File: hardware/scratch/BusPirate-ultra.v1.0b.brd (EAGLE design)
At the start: 100 x 50 mm, 179 parts, among them IC1 23LC1024, IC10 SN74LVC1T45DBV, IC11 SN74LVC1T45DBV, IC12 74LVC1G07DBV, IC13 SN74LVC1T45DBV, IC17 74LVC1G07DBV, IC18 SN74LVC1T45DBV, IC19 74LVC1G07DBV, IC2 23LC1024, IC20 SN74LVC1T45DBV, IC21 74LVC1G07DBV, IC22 SN74LVC1T45DBV, IC23 MCP1824_ADJ, IC24 74HCT4051, IC3 74AC573, IC4 74LVC1G07DBV, IC5 74LVC1G07DBV, IC6 74LVC1G07DBV, IC7 74LVC1G07DBV, IC8 SN74LVC1T45DBV, IC9 SN74LVC1T45DBV, J2 CON_HEADER_1X04, J4 CON_HEADER_1X10-RIGHT_ANGLED_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, Q1 DMMT3906W, U1 W25X40CL, U2 STM32F103ZX, U3 ICE40HX4K, U4 MCP6001, U5 MCP4442, U6 MCP4442, U7 MCP6001

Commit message: change buffer 573 to 244, replaced MCP4446 digital pot back to 4066 analog switch
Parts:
- removed IC3: 74AC573, dp_devices:TSSOP-20
- removed R49, R52: 10K, dp_devices.v6:R603
- added U8: 74HCT4066PW, dp_devices.v6:TSSOP-14
- U5: value MCP4442 -> 74LVC245A; device dp_devices.v6:TSSOP-14 -> dp_devices.v6:TSSOP-20
- U9: value MCP4442 -> 74HCT4066PW
- moved U5 24.3 mm to (76.8, 23.5), turned to 270 degrees
- turned U9 to 0 degrees
- renumbered U6 to U9
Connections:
- removed net MCU_I2C_SCL: R49.1, U2.136, U5.4, U9.4
- removed net MCU_I2C_SDA: R52.1, U2.137, U5.5, U9.5
- removed net N$47: RN3.2, U9.13
- removed net N$48: RN3.4, U9.2
- removed net V33PU: U2.56
- removed net V50PU: U2.57
- new net MCU_VPU: U2.56, U8.12, U8.13, U8.5, U8.6, U9.12, U9.13, U9.5, U9.6
- new net N$33: RN3.3, U9.1
- new net N$45: RN3.4, U9.11
- net 3V3: now also U5.20; no longer IC3.11, IC3.20, R49.2, R52.2, U9.3
- net BPIO0: now also U5.11; no longer IC3.2
- net BPIO1: now also U5.12; no longer IC3.3
- net BPIO2: now also U5.13; no longer IC3.4
- net BPIO3: now also U5.14; no longer IC3.5
- net BPIO4: now also U5.15; no longer IC3.6
- net BPIO5: now also U5.16; no longer IC3.7
- net BPIO6: now also U5.17; no longer IC3.8
- net BPIO7: now also U5.18; no longer IC3.9
- net GND: now also U5.1, U5.10, U5.19, U8.7, U9.7; no longer IC3.1, IC3.10, U5.11, U5.3, U5.6, U9.11, U9.6
- net LAT0: now also U5.9; no longer IC3.19
- net LAT1: now also U5.8; no longer IC3.18
- net LAT2: now also U5.7; no longer IC3.17
- net LAT3: now also U5.6; no longer IC3.16
- net LAT4: now also U5.5; no longer IC3.15
- net LAT5: now also U5.4; no longer IC3.14
- net LAT6: now also U5.3; no longer IC3.13
- net LAT7: now also U5.2; no longer IC3.12
- net N$2: now also U8.1; no longer U5.10
- net N$3: now also U8.4; no longer U5.7
- net N$4: now also U8.8; no longer U5.13
- net N$42: now also RN3.1, U9.4; no longer RN3.3, U9.10
- net N$44: now also RN3.2, U9.8; no longer RN3.1, U9.7
- net N$5: now also U8.11; no longer U5.2
- net VREF/VOUT: now also U8.10, U8.2, U8.3, U8.9, U9.10, U9.2, U9.3; no longer U5.1, U5.14, U5.8, U5.9, U9.1, U9.14, U9.8
- net VUSB: now also U8.14, U9.14; no longer U5.12, U9.12
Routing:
- net V33PU: track 35.2 -> 0.00 mm, vias 1 -> 0
- net V50PU: track 24.5 -> 0.00 mm, vias 1 -> 0
- net MCU_I2C_SCL: track 11.7 -> 0.00 mm
- net MCU_I2C_SDA: track 8.41 -> 0.00 mm

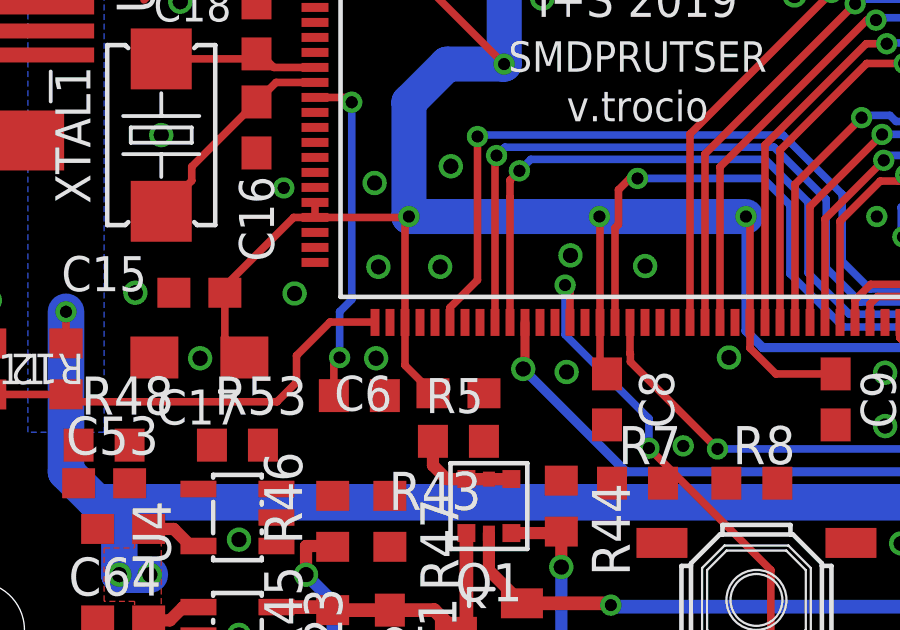
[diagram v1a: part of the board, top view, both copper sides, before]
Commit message: move MCU_AUX12 to pin 55, reserve MCU 41-43 pins for display
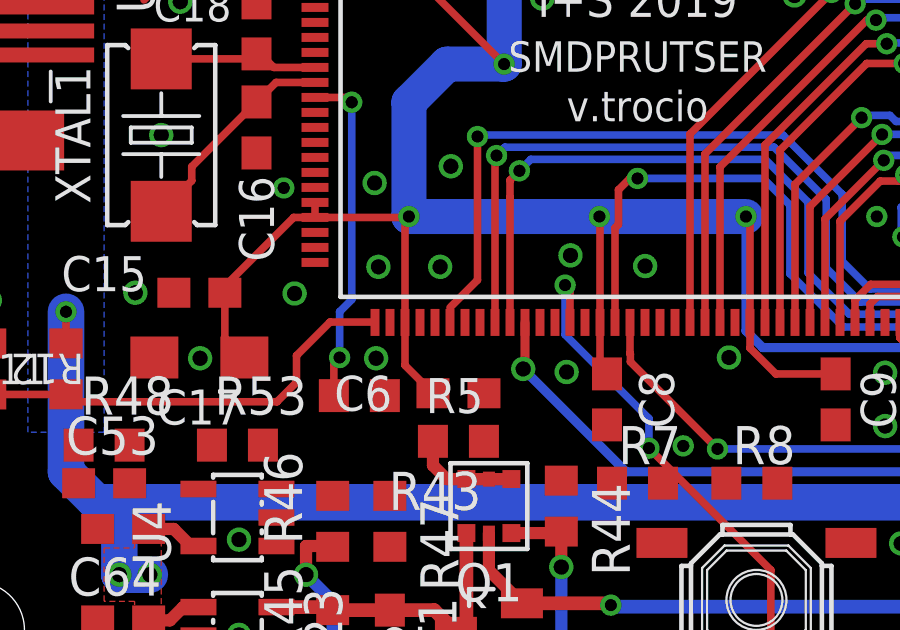
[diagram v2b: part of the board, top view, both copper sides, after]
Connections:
- net ADC2 renamed DISPLAY_SPI_MOSI
- removed net VEXTPU: U2.55
- new net DISPLAY_SPI_CLOCK: U2.41
- new net DISPLAY_SPI_MISO: U2.42
- net MCU_AUX12: now also U2.55; no longer U2.42
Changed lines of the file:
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@@
 <wire x1="61.595" y1="9.271" x2="47.625" y2="2.96" width="0" layer="19" extent="1-16"/>
-</signal>
-<signal name="ADC2">
-<contactref element="U2" pad="43"/>
 </signal>
 <signal name="N$6">
@@
 <wire x1="56.515" y1="6.604" x2="57.15" y2="5.969" width="0.6096" layer="16"/>
 </signal>
-<signal name="VEXTPU">
-<contactref element="U2" pad="55"/>
-</signal>
 <signal name="UART_RX">
 <contactref element="TP2" pad="TP"/>
@@
 <signal name="MCU_AUX12">
 <contactref element="U3" pad="41"/>
-<contactref element="U2" pad="42"/>
 <wire x1="47.3393" y1="14.25" x2="47.3393" y2="15.3987" width="0.254" layer="1"/>
 <wire x1="47.3393" y1="15.3987" x2="46.736" y2="16.002" width="0.254" layer="1"/>
@@
 <wire x1="19.785" y1="14.74513125" x2="20.701" y2="15.66113125" width="0.254" layer="1"/>
 <wire x1="20.701" y1="20.447" x2="20.701" y2="15.66113125" width="0.254" layer="1"/>
-<wire x1="19.785" y1="14.25" x2="19.785" y2="14.74513125" width="0.254" layer="1"/>
 <via x="20.701" y="20.447" extent="1-16" drill="0.4064"/>
 <wire x1="32.8581375" y1="18.523075" x2="30.8834125" y2="20.4978" width="0.254" layer="16"/>
@@
 <wire x1="20.751796875" y1="20.4978" x2="20.701" y2="20.447" width="0.254" layer="16"/>
 <wire x1="46.736" y1="16.002" x2="46.736" y2="16.04066875" width="0.254" layer="16"/>
+<contactref element="U2" pad="55"/>
+<wire x1="20.701" y1="15.66113125" x2="26.285" y2="14.25" width="0" layer="19" extent="1-1"/>
 </signal>
 <signal name="VREF/VOUT">
@@
 <wire x1="26.785" y1="14.25" x2="88.87" y2="9.25" width="0" layer="19" extent="1-1"/>
 </signal>
+<signal name="DISPLAY_SPI_CLOCK">
+<contactref element="U2" pad="41"/>
+</signal>
+<signal name="DISPLAY_SPI_MOSI">
+<contactref element="U2" pad="43"/>
+</signal>
+<signal name="DISPLAY_SPI_MISO">
+<contactref element="U2" pad="42"/>
+</signal>
 </signals>

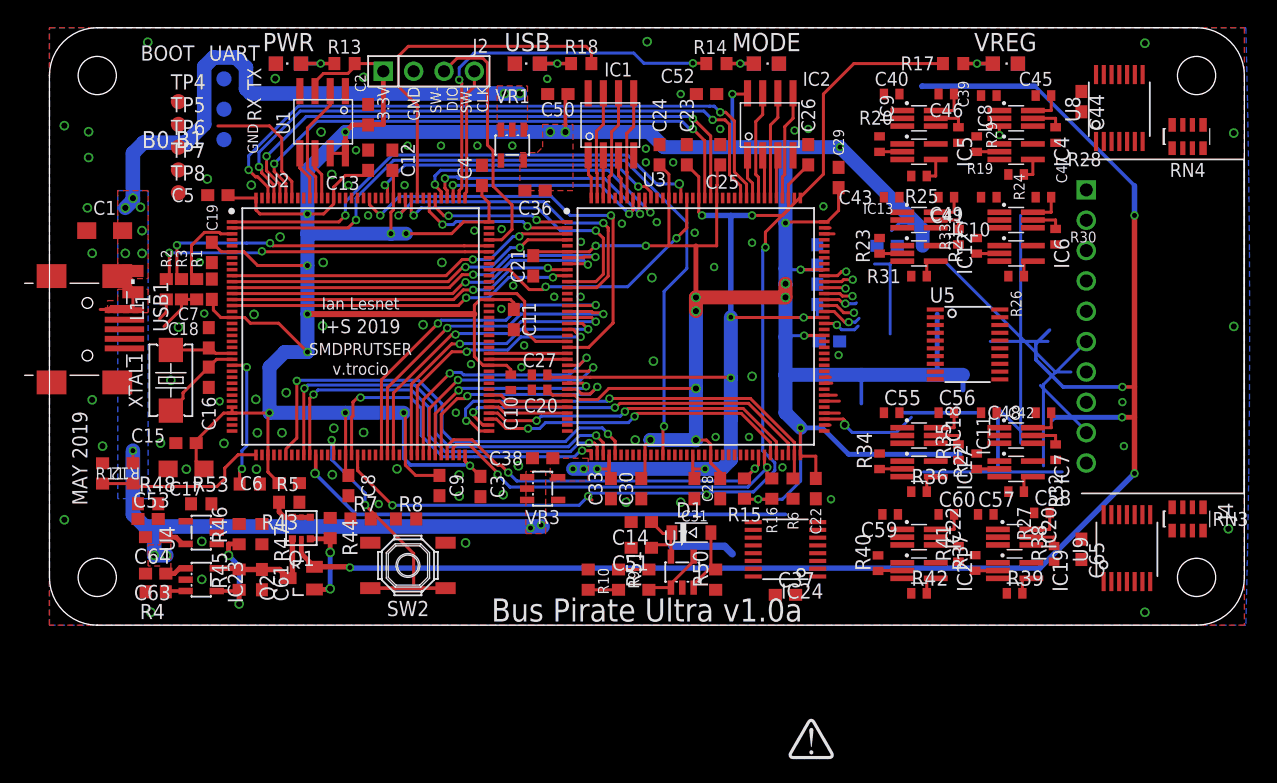
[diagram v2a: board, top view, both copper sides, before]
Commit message: changes in FPGA pin connection *BANK 1
BUFOD0 102
BUFIO0 104
BUFDIR0 101

BUFOD1 106
BUFIO1 107
BUFDIR1 105

BUFOD2 95
BUFIO2 96
BUFDIR2 94

BUFOD3 98
BUFIO3 99
BUFDIR3 97

BUFOD4 80
BUFIO4 81
BUFDIR4 82

BUFOD5 76
BUFIO5 78
BUFDIR5 79

BUFOD6 73
BUFIO6 74
BUFDIR6 75

LAT0 93
LAT1 91
LAT2 90
LAT3 88
LAT4 87
LAT5 85
LAT6 84
LAT7 83

*BANK 2

BUFOD7 62
BUFIO7 63
BUFDIR7 64

ADC_MUX_EN 61
ADC_MUX_S2 60
ADC_MUX_S1 56
ADC_MUX_S0 55
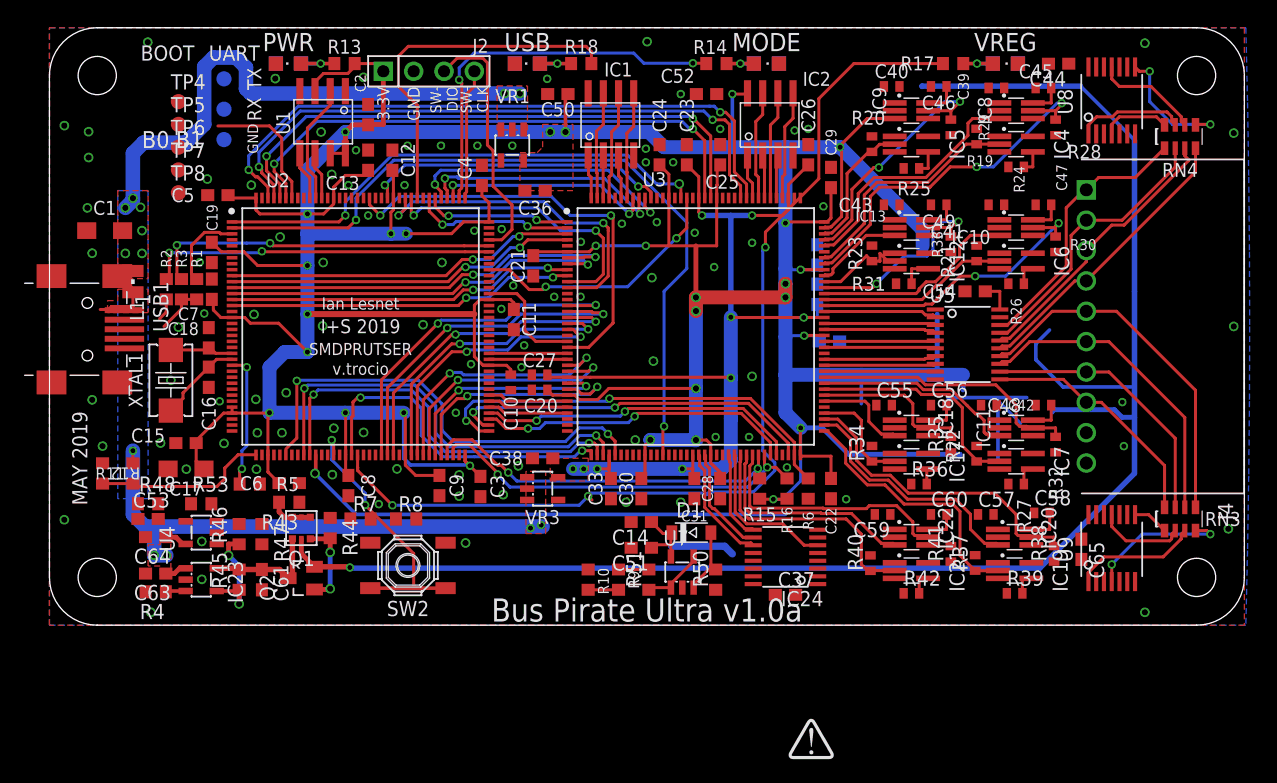
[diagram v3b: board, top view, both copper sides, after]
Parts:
- moved C54 8.29 mm to (77.5, 27.9), flipped to the top
- moved C44 3.70 mm to (84.5, 47.0), turned to 180 degrees
- moved R31 1.42 mm to (71.5, 28.6)
- moved R15 1.27 mm to (59.4, 11.4)
- moved R16 1.27 mm to (61.7, 11.4)
- moved R6 1.27 mm to (63.5, 11.4)
- moved C22 1.27 mm to (65.4, 11.4)
- moved U9 1.27 mm to (88.9, 6.35)
- moved IC18 0.90 mm to (72.1, 16.5)
- moved IC17 0.90 mm to (72.1, 13.7)
- moved C39 0.90 mm to (79.2, 45.0)
- moved C41 0.90 mm to (79.2, 35.2)
- moved C46 0.90 mm to (74.4, 45.1)
- moved C49 0.90 mm to (74.4, 35.2)
- moved C55 0.90 mm to (69.8, 18.4)
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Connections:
- net ADC_MUX_EN: now also U3.61; no longer U3.45
- net ADC_MUX_S0: now also U3.55; no longer U3.42
- net ADC_MUX_S1: now also U3.56; no longer U3.43
- net ADC_MUX_S2: now also U3.60; no longer U3.44
- net BPIO0: now also U5.18; no longer U5.11
- net BPIO1: now also U5.17; no longer U5.12
- net BPIO2: now also U5.16; no longer U5.13
- net BPIO3: now also U5.15; no longer U5.14
- net BPIO4: now also RN3.5, U5.14; no longer RN3.6, U5.15
- net BPIO5: now also RN3.6, U5.13; no longer RN3.8, U5.16
- net BPIO6: now also U5.12; no longer U5.17
- net BPIO7: now also RN3.8, U5.11; no longer RN3.5, U5.18
- net BUFDIR0: now also U3.101; no longer U3.79
- net BUFDIR1: now also U3.105; no longer U3.75
- net BUFDIR2: now also U3.94; no longer U3.82
- net BUFDIR3: now also U3.97; no longer U3.107
- net BUFDIR4: now also U3.82; no longer U3.104
- net BUFDIR5: now also U3.79; no longer U3.88
- net BUFDIR6: now also U3.75; no longer U3.61
- net BUFIO0: now also U3.104; no longer U3.78
- net BUFIO1: now also U3.107; no longer U3.74
- net BUFIO2: now also U3.96; no longer U3.81
- net BUFIO3: now also U3.99; no longer U3.106
- net BUFIO4: now also U3.81; no longer U3.102
- net BUFIO5: now also U3.78; no longer U3.87
- net BUFIO6: now also U3.74; no longer U3.60
- net BUFOD0: now also U3.102; no longer U3.76
- net BUFOD1: now also U3.106; no longer U3.73
- net BUFOD2: now also U3.95; no longer U3.80
- net BUFOD3: now also U3.98; no longer U3.105
- net BUFOD4: now also U3.80; no longer U3.101
- net BUFOD5: now also U3.76; no longer U3.85
- net BUFOD6: now also U3.73; no longer U3.56
- net LAT0: now also U3.93, U5.2; no longer U3.99, U5.9
- net LAT1: now also U3.91, U5.3; no longer U3.98, U5.8
- net LAT2: now also U3.90, U5.4; no longer U3.97, U5.7
- net LAT3: now also U3.88, U5.5; no longer U3.96, U5.6
- net LAT4: now also U3.87, U5.6; no longer U3.95, U5.5
- net LAT5: now also U3.85, U5.7; no longer U3.94, U5.4
- net LAT6: now also U3.84, U5.8; no longer U3.93, U5.3
- net LAT7: now also U3.83, U5.9; no longer U3.91, U5.2
- net N$2: now also RN4.7; no longer RN4.6
- net N$3: now also RN4.8; no longer RN4.5
- net N$4: now also RN4.5; no longer RN4.8
- net N$42: now also RN3.4; no longer RN3.1
- net N$44: now also RN3.1; no longer RN3.2
- net N$45: now also RN3.2; no longer RN3.4
- net N$5: now also RN4.6; no longer RN4.7
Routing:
- net BPIO4: track 2.00 -> 32.5 mm
- net BUFDIR0: track 3.66 -> 30.3 mm, vias 0 -> 2
- net BUFDIR6: track 2.65 -> 26.1 mm
- net BPIO0: track 2.00 -> 24.8 mm
- net BPIO6: track 2.01 -> 24.8 mm
- net BUFDIR7: track 0.00 -> 21.2 mm
- net BUFIO6: track 0.00 -> 20.5 mm
- net BUFOD6: track 1.92 -> 22.2 mm
- net BPIO7: track 2.01 -> 22.3 mm
- net BUFOD7: track 2.06 -> 21.2 mm
- net BPIO2: track 6.70 -> 25.8 mm
- net BUFIO0: track 2.02 -> 21.0 mm, vias 1 -> 0
- net BUFIO7: track 0.00 -> 18.3 mm
- net BUFDIR2: track 7.98 -> 25.6 mm, vias 0 -> 2
- net BUFOD4: track 1.92 -> 19.1 mm
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
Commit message: remove UART and Flash TPs, remove remaining switch, move vreg circuit
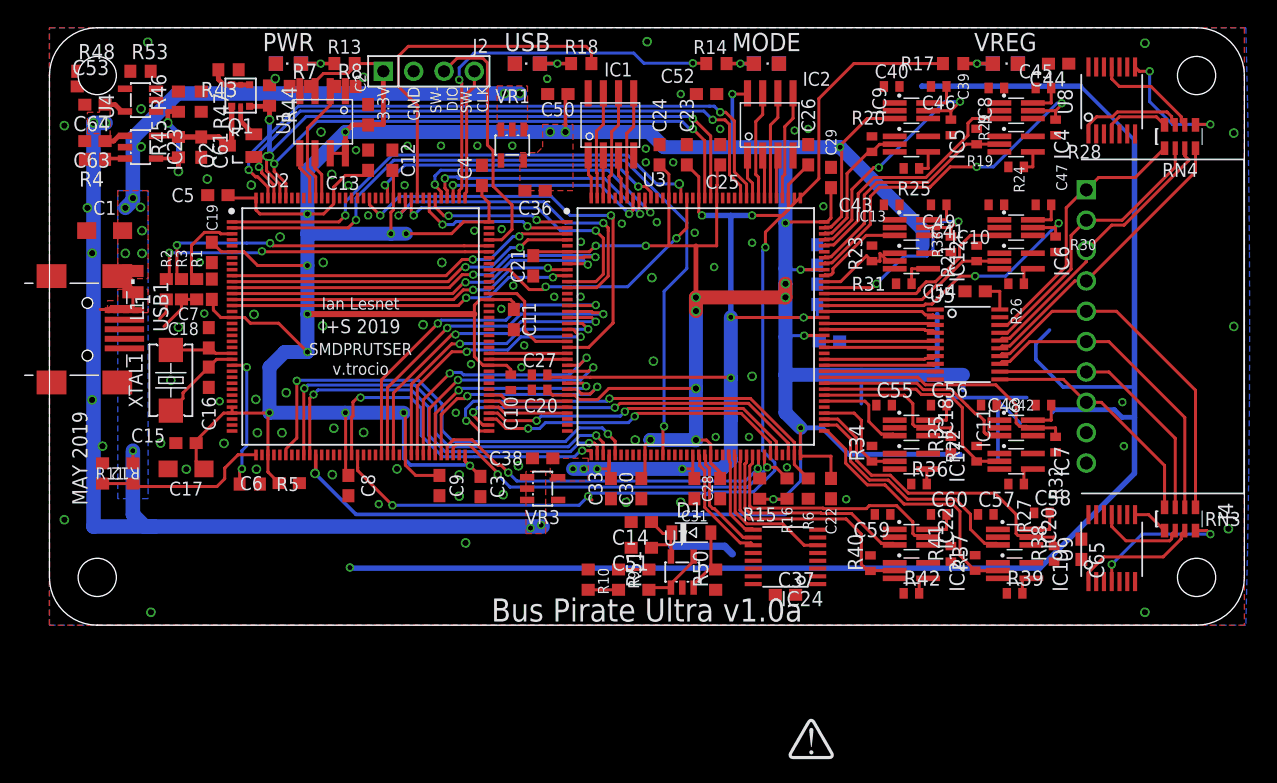
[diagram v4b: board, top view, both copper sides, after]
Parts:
- removed SW2: (no value), dp_devices.v6:SW_TACT_SMALL
- removed TP1, TP2, TP3, TP4, TP5, TP6, TP7, TP8: TPB1,27, testpad:B1,27
- moved C53 36.5 mm to (3.17, 45.1)
- moved C61 36.5 mm to (12.7, 40.0)
- moved C63 36.5 mm to (3.81, 40.5)
- moved C64 36.5 mm to (3.81, 43.6)
- moved IC23 36.5 mm to (7.62, 40.0)
- moved Q1 36.5 mm to (16.0, 44.3)
- moved Q2 36.5 mm to (16.0, 40.1)
- moved R4 36.5 mm to (3.81, 39.0)
- moved R43 36.5 mm to (15.0, 46.5)
- moved R44 36.5 mm to (18.4, 44.3)
- moved R45 36.5 mm to (10.8, 40.0)
- moved R46 36.5 mm to (10.8, 43.8)
- moved R47 36.5 mm to (12.7, 43.8)
- moved R7 36.5 mm to (21.0, 45.1)
- moved R8 36.5 mm to (24.8, 45.1)
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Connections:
- removed net MS0: SW2.1, SW2.2, U2.50
- net FLASH_CS: no longer TP7.TP
- net FLASH_MISO: no longer TP5.TP
- net FLASH_MOSI: no longer TP4.TP
- net FLASH_SCK: no longer TP6.TP
- net GND: no longer SW2.3, SW2.4, TP1.TP, TP8.TP
- net UART_RX: no longer TP2.TP
- net UART_TX: no longer TP3.TP
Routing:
- net VUSB: track 100.0 -> 130.8 mm
- net MS0: track 22.8 -> 0.00 mm, vias 2 -> 0
- net GND: track 11.6 -> 0.44 mm, vias 98 -> 96
- net VREF/VOUT: track 171.1 -> 168.0 mm
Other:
- board text removed: "B0"
- board text removed: "B1"
- board text removed: "BOOT"
- board text removed: "RX"
- board text removed: "TX"
- board text removed: "UART"
